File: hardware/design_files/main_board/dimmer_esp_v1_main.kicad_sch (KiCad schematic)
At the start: 42 parts, among them J1 SM05B-SRSS-TB_LF__SN_, J3 Plug_1, J4 Conn_01x02, J5 Conn_01x02, J6 Conn_01x02, J7 Conn_01x04, SW2 Encoder Button, U1 Encoder: PES12-40S-N0024, U2 LDO: SPX3819M5-L-3-3, U3 ESP32-C6-MINI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

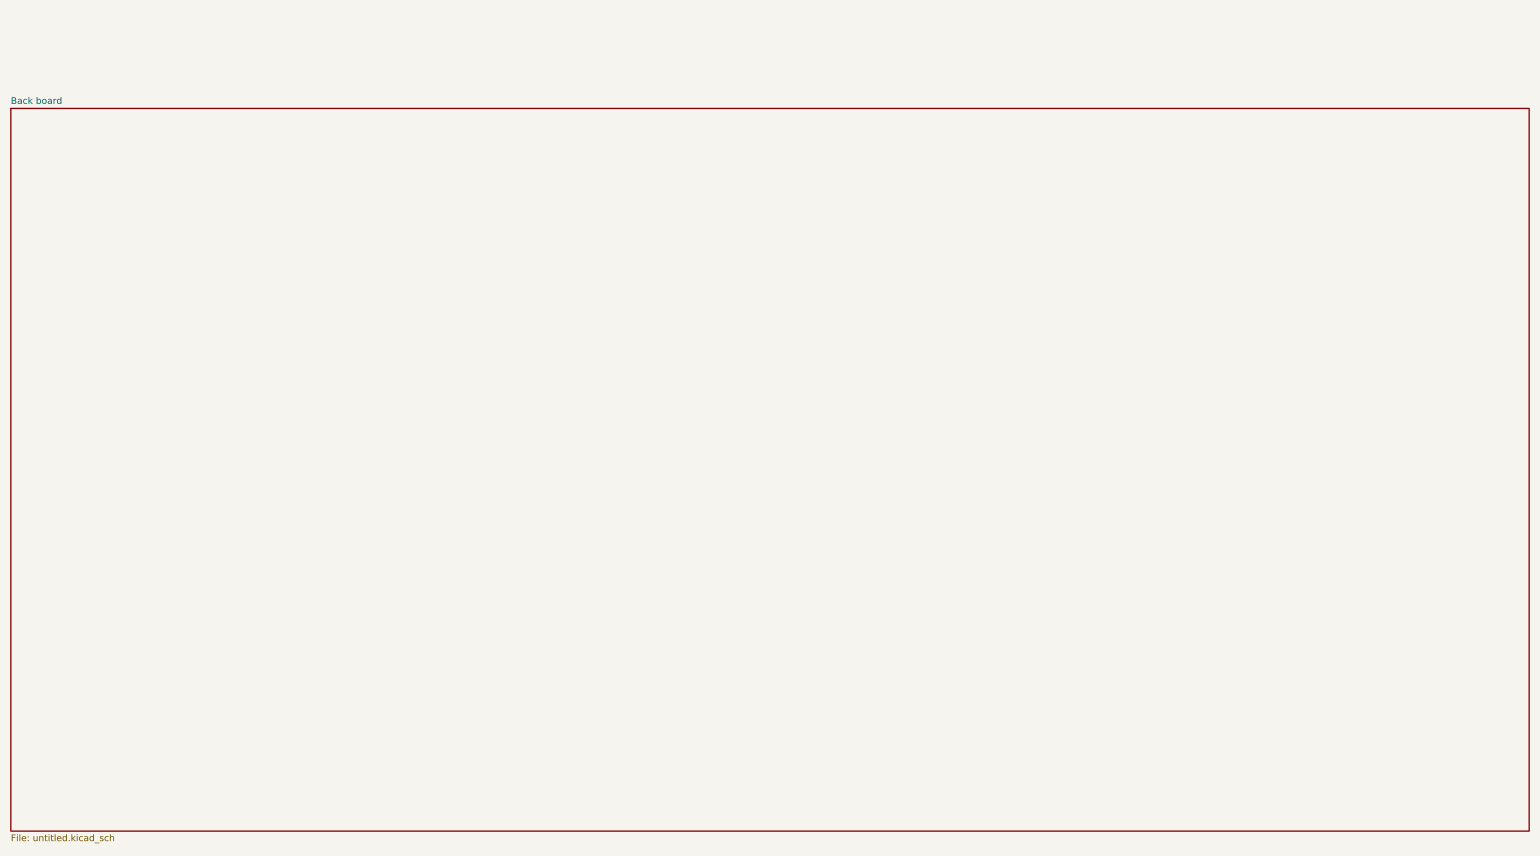
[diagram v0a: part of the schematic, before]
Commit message: Remove unused second page from schematics
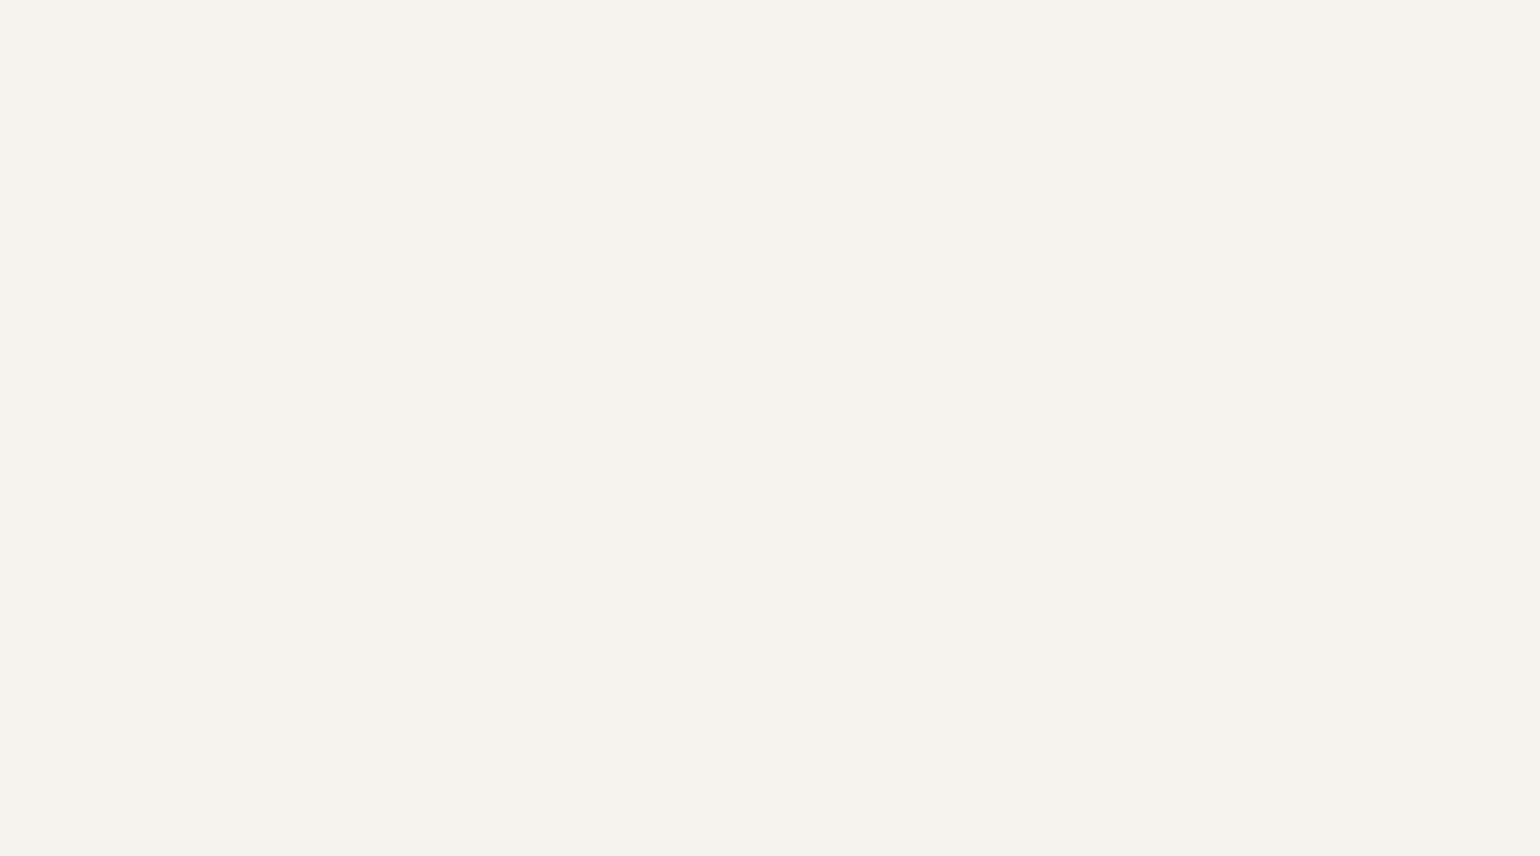
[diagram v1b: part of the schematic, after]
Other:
- removed sheet Back board
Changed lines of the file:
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@@
-		)
-	)
-	(sheet
-		(at 8.89 236.22)
-		(size 290.83 138.43)
-		(fields_autoplaced yes)
-		(stroke
-			(width 0.1524)
-			(type solid)
-		)
-		(fill
-			(color 0 0 0 0.0000)
-		)
-		(property "Sheetname" "Back board"
-			(at 8.89 235.5084 0)
-			(effects
-				(font
-					(size 1.27 1.27)
-				)
-				(justify left bottom)
-			)
-		)
-		(property "Sheetfile" "untitled.kicad_sch"
-			(at 8.89 375.2346 0)
-			(effects
-				(font
-					(size 1.27 1.27)
-				)
-				(justify left top)
-			)
-		)
-		(instances
-			(project "dimmer_esp_v1_main"
-				(path "/ddfcd425-273c-4c73-9404-db5c5faab60e"
-					(page "2")
-				)
-			)
 		)
 	)

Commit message: Save as kicad 9.0.2, update libraries
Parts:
- D3: footprint SparkFun-LED:WS2812_5050-4Pin -> LED_SMD:LED_WS2812B_PLCC4_5.0x5.0mm_P3.2mm
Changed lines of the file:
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@@
 (kicad_sch
-	(version 20231120)
+	(version 20250114)
 	(generator "eeschema")
-	(generator_version "8.0")
+	(generator_version "9.0")
 	(paper "A4")
 	(junction
@@
 	(label "UART_RXD"
 		(at 262.89 123.19 180)
-		(fields_autoplaced yes)
 		(effects
 			(font
@@
 	(label "UART_RXD"
 		(at 227.33 87.63 0)
-		(fields_autoplaced yes)
 		(effects
 			(font
@@
 	(label "D15"
 		(at 257.81 69.85 0)
-		(fields_autoplaced yes)
 		(effects
 			(font
@@
 	(label "D22"
 		(at 27.94 50.8 0)
-		(fields_autoplaced yes)
 		(effects
 			(font
@@
 	(label "UART_TXD"
 		(at 262.89 125.73 180)
-		(fields_autoplaced yes)
 		(effects
 			(font
@@
 	(label "D09"
 		(at 57.15 143.51 0)
-		(fields_autoplaced yes)
 		(effects
 			(font
@@
 	(label "D18"
 		(at 257.81 87.63 0)
-		(fields_autoplaced yes)
 		(effects
 			(font
@@
 	(label "D19"
 		(at 246.38 104.14 180)
-		(fields_autoplaced yes)
 		(effects
 			(font
@@
 	(label "EN"
 		(at 262.89 130.81 180)
-		(fields_autoplaced yes)
 		(effects
 			(font
@@
 	(label "D06"
 		(at 194.31 63.5 180)
-		(fields_autoplaced yes)
 		(effects
 			(font
@@
 	(label "D12"
 		(at 128.27 73.66 0)
-		(fields_autoplaced yes)
 		(effects
 			(font
@@
 	(label "D18"
 		(at 194.31 86.36 180)
-		(fields_autoplaced yes)
 		(effects
 			(font
@@
 	(label "D13"
 		(at 194.31 71.12 180)
-		(fields_autoplaced yes)
 		(effects
 			(font
@@
 	(label "D20"
 		(at 194.31 91.44 180)
-		(fields_autoplaced yes)
 		(effects
 			(font
@@
 	(label "D12"
 		(at 194.31 68.58 180)
-		(fields_autoplaced yes)
 		(effects
 			(font
@@
 	(label "D01"
 		(at 195.58 140.97 180)
-		(fields_autoplaced yes)
 		(effects
 			(font
@@
 	(label "D21"
 		(at 26.67 27.94 0)
-		(fields_autoplaced yes)
 		(effects
 			(font
@@
 	(label "D06"
 		(at 246.38 99.06 180)
-		(fields_autoplaced yes)
 		(effects
 			(font
@@
 	(label "UART_TXD"
 		(at 227.33 85.09 0)
-		(fields_autoplaced yes)
 		(effects
 			(font
@@
 	(label "EN"
 		(at 146.05 120.65 0)
-		(fields_autoplaced yes)
 		(effects
 			(font
@@
 	(label "D14"
 		(at 194.31 73.66 180)
-		(fields_autoplaced yes)
 		(effects
 			(font
@@
 	(label "D09"
 		(at 262.89 128.27 180)
-		(fields_autoplaced yes)
 		(effects
 			(font
@@
 	(label "D09"
 		(at 194.31 83.82 180)
-		(fields_autoplaced yes)
 		(effects
 			(font
@@
 	(label "D19"
 		(at 194.31 88.9 180)
-		(fields_autoplaced yes)
 		(effects
 			(font
@@
 	(label "D22"
 		(at 227.33 92.71 0)
-		(fields_autoplaced yes)
 		(effects
 			(font
@@
 	(label "D14"
 		(at 257.81 50.8 0)
-		(fields_autoplaced yes)
 		(effects
 			(font
@@
 	(label "D07"
 		(at 246.38 101.6 180)
-		(fields_autoplaced yes)
 		(effects
 			(font
@@
 	(label "D15"
 		(at 194.31 76.2 180)
-		(fields_autoplaced yes)
 		(effects
 			(font
@@
 	(label "D01"
 		(at 194.31 58.42 180)
-		(fields_autoplaced yes)
 		(effects
 			(font
@@
 	(label "D13"
 		(at 128.27 76.2 0)
-		(fields_autoplaced yes)
 		(effects
 			(font
@@
 	(label "EN"
 		(at 194.31 45.72 180)
-		(fields_autoplaced yes)
 		(effects
 			(font
@@
 	(label "D07"
 		(at 194.31 66.04 180)
-		(fields_autoplaced yes)
 		(effects
 			(font
@@
 	(label "D21"
 		(at 194.31 93.98 180)
-		(fields_autoplaced yes)
 		(effects
 			(font
@@
 	(label "D20"
 		(at 85.09 30.48 0)
-		(fields_autoplaced yes)
 		(effects
 			(font
@@
 			)
 		)
-		(property "Footprint" "SparkFun-LED:WS2812_5050-4Pin"
+		(property "Footprint" "LED_SMD:LED_WS2812B_PLCC4_5.0x5.0mm_P3.2mm"
 			(at 228.6 149.86 0)
 			(effects
@@
 		)
 	)
+	(embedded_fonts no)
 )

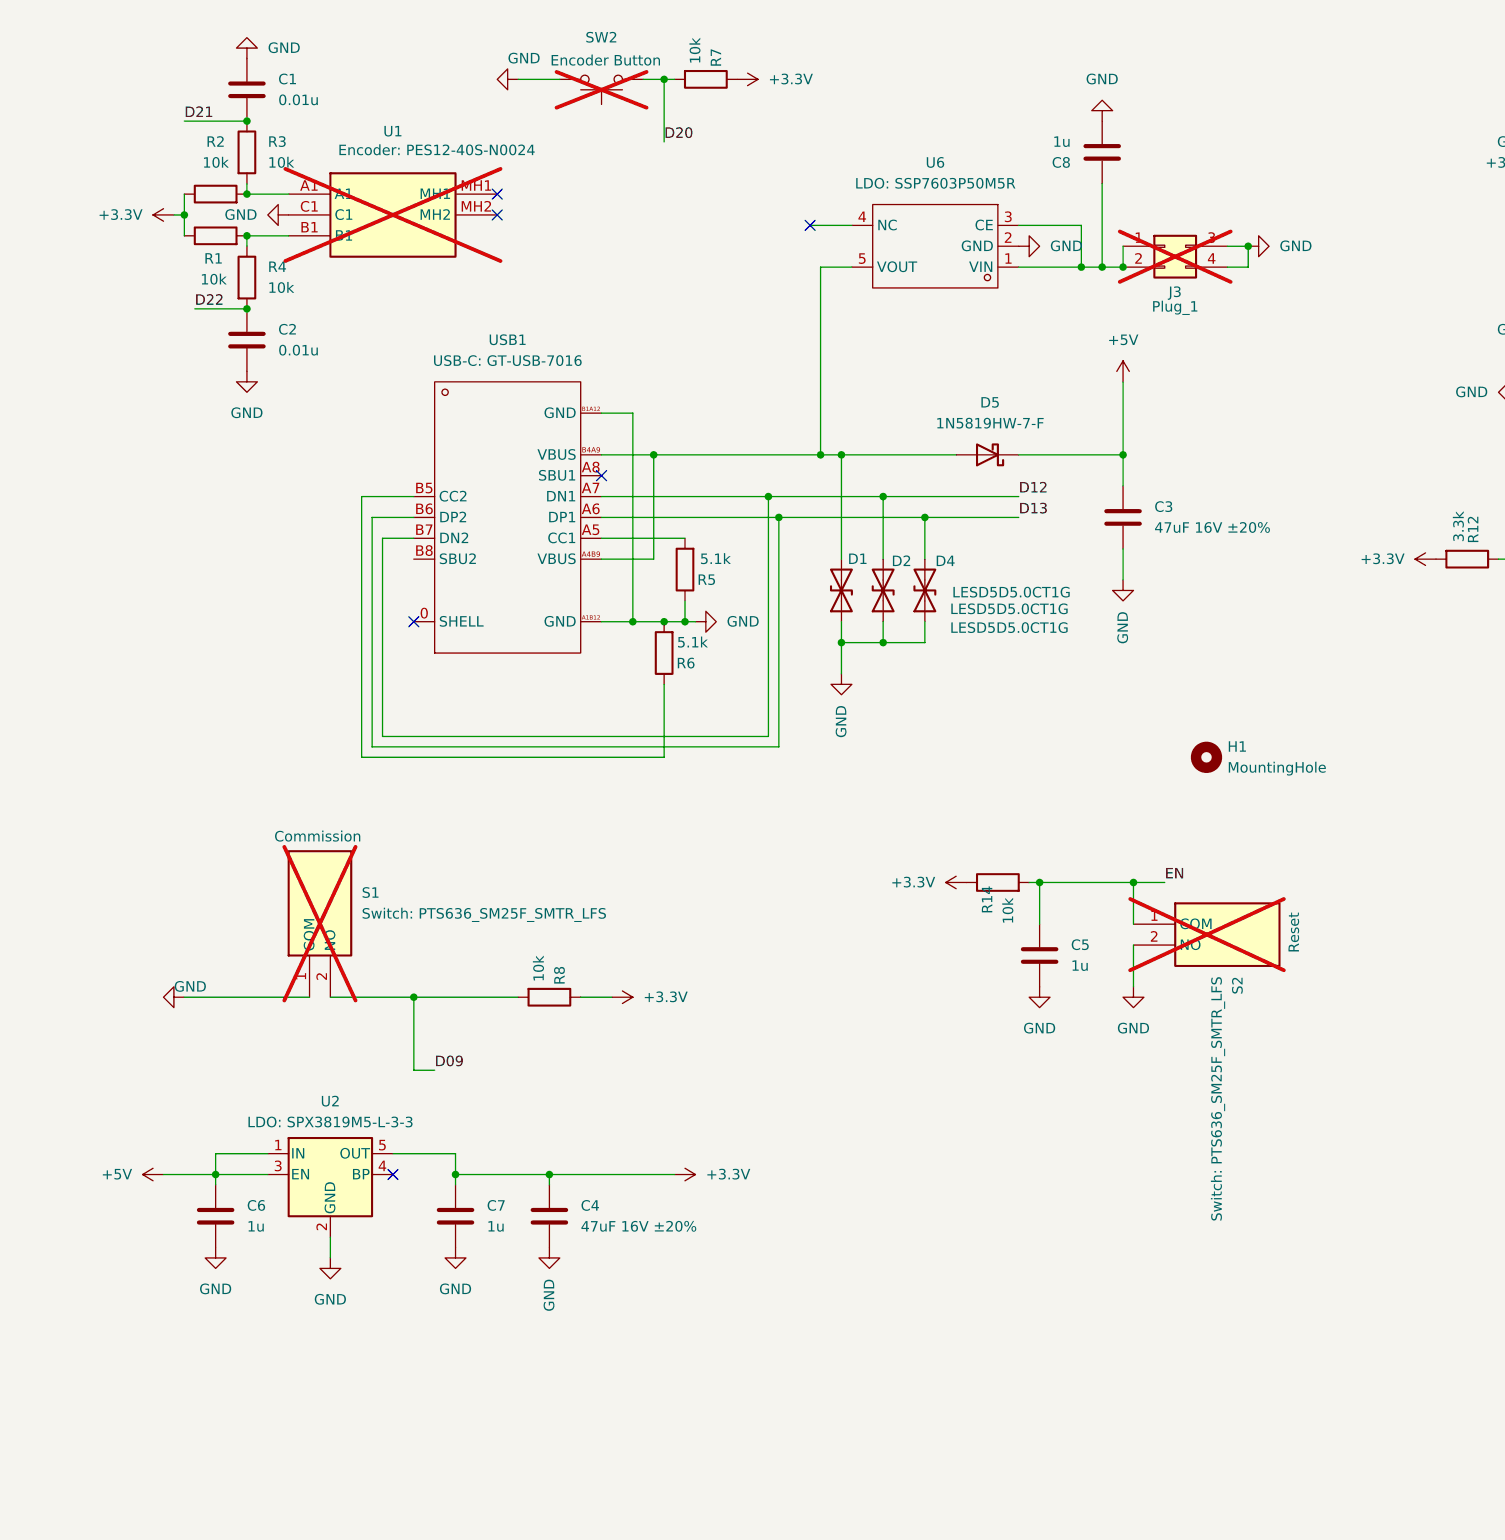
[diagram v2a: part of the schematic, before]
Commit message: Add components, version with relay, needs re-layout of tracks
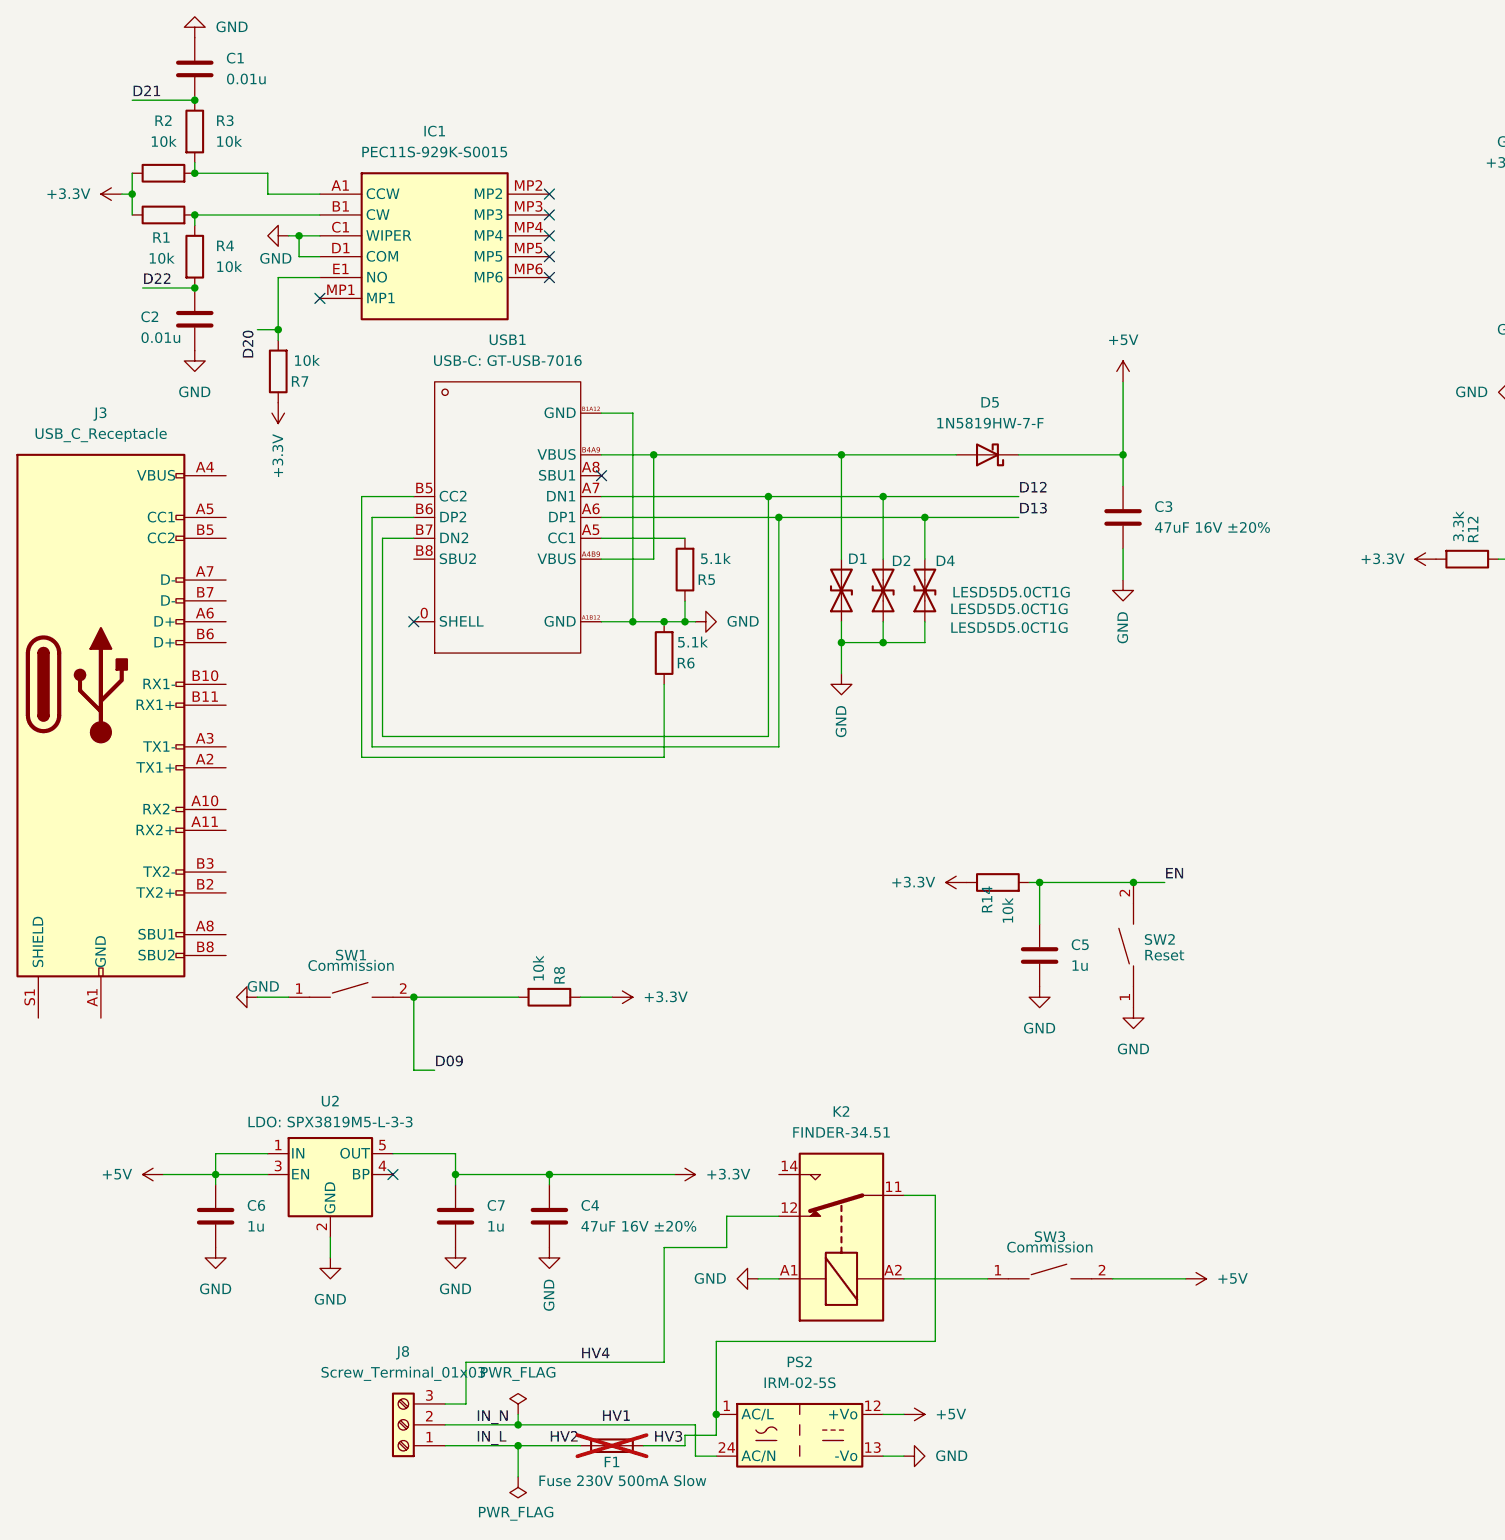
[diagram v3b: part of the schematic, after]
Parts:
- removed C8: 1u, Capacitor_SMD:C_0603_1608Metric, symbol Device:C
- removed H1: MountingHole, MountingHole:MountingHole_2.2mm_M2_DIN965, symbol Mechanical:MountingHole
- removed J3: Plug_1, Connector_PinHeader_2.54mm:PinHeader_2x02_P2.54mm_Vertical, symbol Connector_Generic:Conn_02x02_Top_Bottom
- removed S1, S2: Switch: PTS636_SM25F_SMTR_LFS, button_ck:PTS636_SM25F_SMTR_LFS, symbol button_ck:PTS636_SM25F_SMTR_LFS
- removed SW2: Encoder Button, button_diptronics:TAEF25SVTR, symbol Switch:SW_Push
- removed U1: Encoder: PES12-40S-N0024, bourns_encoder:PES1240SN0024, symbol bourns:PES12-40S-N0024
- removed U6: LDO: SSP7603P50M5R, Package_TO_SOT_SMD:SOT-23-5, symbol ldo_jlcpcb:SSP7603P50M5R
- added F1: Fuse 230V 500mA Slow, jlc_misc:0443.500DR, symbol Device:Fuse
- added IC1: PEC11S-929K-S0015, bourns_encoder:PEC11S929KS0015, symbol bourns:PEC11S-929K-S0015
- added J3: USB_C_Receptacle, Connector_USB:USB_C_Receptacle_JAE_DX07S024WJ3R400, symbol Connector:USB_C_Receptacle
- added J8: Screw_Terminal_01x03, TerminalBlock_Phoenix:TerminalBlock_Phoenix_MKDS-1,5-3-5.08_1x03_P5.08mm_Horizontal, symbol Connector:Screw_Terminal_01x03
- added K2: FINDER-34.51, Relay_THT:Relay_SPDT_Finder_34.51_Vertical, symbol Relay:FINDER-34.51
- added PS2: IRM-02-5S, Converter_ACDC:Converter_ACDC_MeanWell_IRM-02-xx_SMD, symbol Converter_ACDC:IRM-02-5S
- added SW1, SW3: Commission, button_jlc:SW-SMD_L3.9-W3.0-P4.45, symbol button_ck:TS-1088-AR02016
- added SW2: Reset, button_jlc:SW-SMD_L3.9-W3.0-P4.45, symbol button_ck:TS-1088-AR02016
- C1, C2: footprint Capacitor_SMD:C_0402_1005Metric -> Capacitor_SMD:C_0603_1608Metric
- R1, R10, R11, R14, R2, R3, R4, R7, R8, R9: footprint Resistor_SMD:R_0402_1005Metric -> Resistor_SMD:R_0603_1608Metric
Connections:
- net +5V: now also PS2.12 (+Vo), SW3.2
- net D09: now also SW1.2
- net D20: now also IC1.E1 (NO)
- net EN: now also SW2.2
- net GND: now also IC1.C1 (WIPER), IC1.D1 (COM), K2.A1, PS2.13 (-Vo), SW1.1, SW2.1
- net at R2.2, R3.2: now also IC1.A1 (CCW)
- net at R1.2, R4.1: now also IC1.B1 (CW)
- new net: K2.A2, SW3.1
- new net: J3.A1 (GND), J3.A12 (GND), J3.B1 (GND), J3.B12 (GND)
- new net: J3.A4 (VBUS), J3.A9 (VBUS), J3.B4 (VBUS), J3.B9 (VBUS)
- new net HV1: J8.2 (Pin_2), PS2.24 (AC/N)
- new net HV2: F1.2, J8.1 (Pin_1)
- new net HV3: F1.1, K2.11, PS2.1 (AC/L)
- new net HV4: J8.3 (Pin_3), K2.12
- no-connect marks 16 -> 19
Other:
- moved on the sheet: C1, C2, R1, R2, R3, R4, R7
